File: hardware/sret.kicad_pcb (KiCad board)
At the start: 4 copper layers, 87.9 x 54.4 mm, 105 parts, among them CON1 SD_Card, J1 RJ45-TRANSFO, P1 USB0, P10 CONN_02X04, P11 USB1, P12 CONN_02X01, P13 CONN_02X01, P2 CONN_02X01, P3 CONN_02X01, P4 CONN_02X01, P5 CONN_02X01, P6 CONN_01X06, P7 CONN_01X06, P8 CONN_01X06, P9 CONN_01X06, SW1 DFU, SW2 RESET, U1 LPC4330, U2 DRTR5V0U2SR, U3 W25Q80BV, U4 LAN8742A, U5 MAX3051, U6 MAX3051, U7 TC1262, X1 CRYSTAL_SMD, X2 CRYSTAL_SMD, Y1 RTC

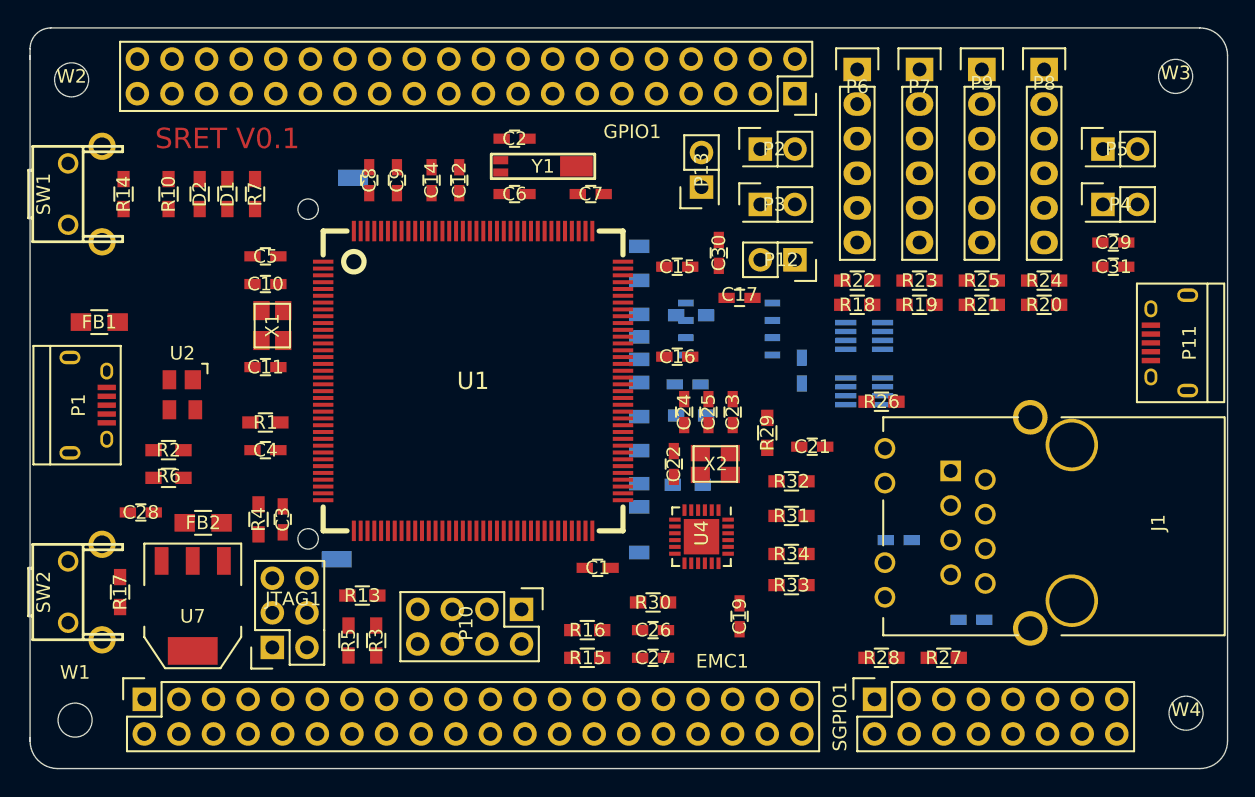
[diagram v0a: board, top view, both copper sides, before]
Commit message: added RS485/IEBus chip
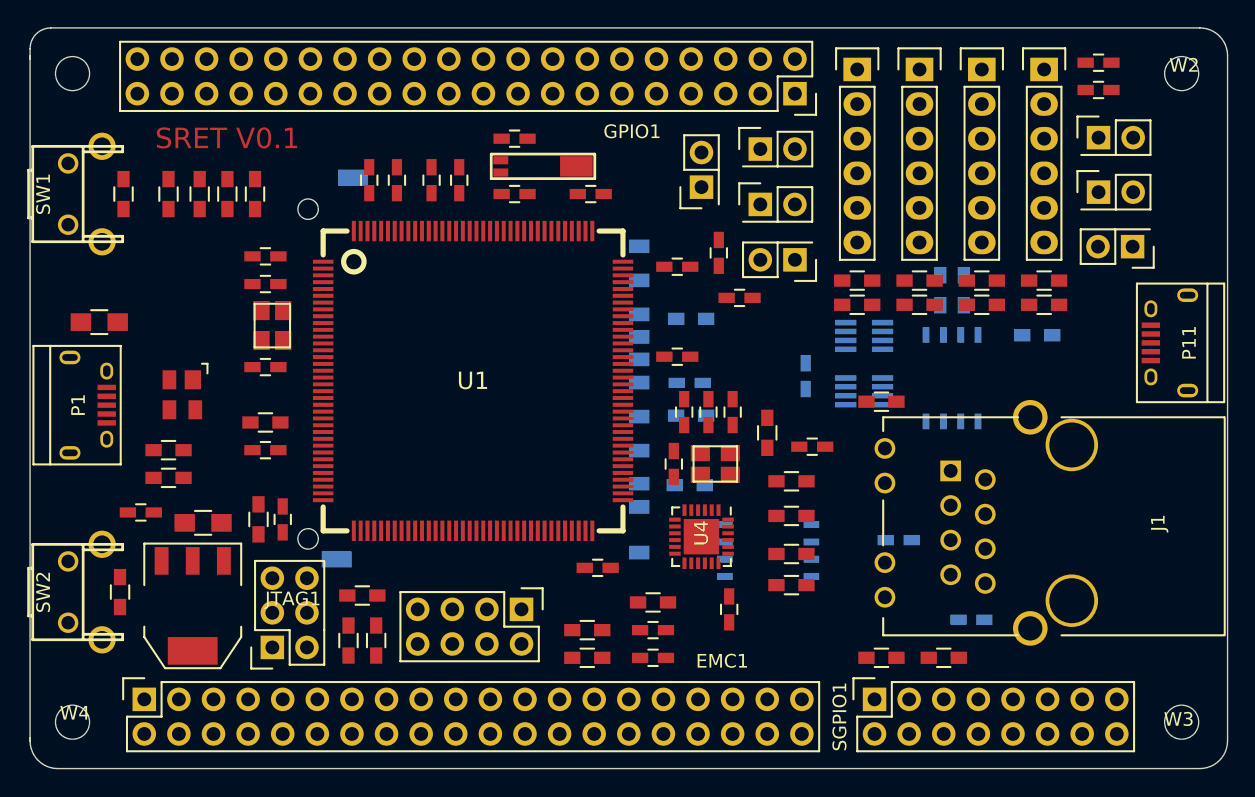
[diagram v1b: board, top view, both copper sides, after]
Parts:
- added P14: CONN_02X01, Pin_Headers:Pin_Header_Straight_2x01, F.Cu at (118.0, 44.5)
- added R12: 10k, Resistors_SMD:R_0603_HandSoldering, B.Cu at (111.0, 51.0)
- added R35: 180, Resistors_SMD:R_0603_HandSoldering, B.Cu at (105.6, 47.7)
- added R36: 180, Resistors_SMD:R_0603_HandSoldering, B.Cu at (103.9, 47.7)
- added U8: RS-485/IEBus, SMD_Packages:SOIC-8-N, B.Cu at (104.7, 54.2)
- moved W4 81.7 mm to (40.2, 79.4)
- moved W2 81.5 mm to (121.6, 31.8)
- moved W1 47.4 mm to (40.2, 31.8)
- moved W3 47.4 mm to (121.6, 79.4)
- moved U3 16.5 mm to (91.2, 66.8)
- moved C31 15.0 mm to (115.5, 31.0), turned to 180 degrees
- moved C29 11.2 mm to (115.5, 33.0), turned to 180 degrees
- moved P4 0.96 mm to (115.5, 40.5)
- moved C19 0.92 mm to (88.4, 71.1)
- moved P5 0.90 mm to (115.5, 36.5)
- moved C13 0.49 mm to (94.0, 54.0)
- moved R8 0.27 mm to (85.6, 49.8)
- moved C32 0.19 mm to (85.5, 54.5)
- moved R11 0.16 mm to (85.5, 62.0)
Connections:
- EMC1 pad 40: GND -> VCC
- GPIO1 pad 23: GND -> /A
- GPIO1 pad 25: /ALARM -> /B
- GPIO1 pad 39: VCC -> GND
- SGPIO1 pad 15: GND -> /ALARM

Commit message: pcb routing started
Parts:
- removed ?: Symbol_OSHW-Logo_SilkScreen, Symbols:Symbol_OSHW-Logo_SilkScreen
- removed EMC1, GPIO1: CONN_02X20, Socket_Strips:Socket_Strip_Straight_2x20
- removed SGPIO1: CONN_02X08, Socket_Strips:Socket_Strip_Straight_2x08
- added EMC: CONN_02X20, Socket_Strips:Socket_Strip_Straight_2x20, F.Cu at (45.3, 78.0)
- added GPIO: CONN_02X20, Socket_Strips:Socket_Strip_Straight_2x20, F.Cu at (45.3, 30.9)
- added SGPIO: CONN_02X08, Socket_Strips:Socket_Strip_Straight_2x08, F.Cu at (98.5, 77.9)
- C1: moved to B.Cu
- P1, P11: footprint Connect:USB_Micro-B -> Connect:USB_Micro-B_circle
- moved U2 4.26 mm to (48.9, 51.1), turned to 270 degrees
- moved C1 2.53 mm to (77.9, 70.5), turned to 270 degrees
- moved R30 1.77 mm to (81.8, 69.1), turned to 270 degrees
- moved R11 1.19 mm to (85.5, 60.8)
- moved C19 1.05 mm to (89.4, 71.5)
- moved C26 0.95 mm to (83.1, 73.5), turned to 0 degrees
- moved R16 0.92 mm to (77.3, 73.3)
- moved C23 0.84 mm to (89.3, 56.1)
- moved R15 0.81 mm to (77.3, 75.2)
- moved X2 0.75 mm to (87.4, 59.7)
- moved C27 0.64 mm to (83.1, 75.2), turned to 0 degrees
- moved SW1 0.62 mm to (40.5, 40.7)
- moved SW2 0.62 mm to (40.5, 69.9)
- moved C11 0.59 mm to (53.8, 53.2)
- moved C10 0.58 mm to (53.8, 47.3), turned to 180 degrees
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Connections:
- U1 pad 7: (no net) -> /GPIO1
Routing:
- net VCC: track 0.00 -> 71.8 mm, vias 0 -> 2
- net /ENET_MDC: track 0.00 -> 42.5 mm, vias 0 -> 4
- net /ENET_TX_EN: track 0.00 -> 41.9 mm, vias 0 -> 4
- net Net-(J1-PadYA): track 0.00 -> 28.1 mm, vias 0 -> 3
- net /ENET_RXD1: track 0.00 -> 27.2 mm
- net Net-(J1-Pad4): track 0.00 -> 23.4 mm, vias 0 -> 1
- net /5V: track 0.00 -> 22.3 mm
- net Net-(J1-Pad6): track 0.00 -> 21.8 mm, vias 0 -> 1
- net Net-(J1-Pad3): track 0.00 -> 21.0 mm
- net Net-(J1-Pad1): track 0.00 -> 20.9 mm
- net /ENET_TXD1: track 0.00 -> 20.8 mm, vias 0 -> 2
- net /ENET_TXD0: track 0.00 -> 20.7 mm, vias 0 -> 4
- net Net-(P1-Pad3): track 0.00 -> 19.8 mm, vias 0 -> 2
- net Net-(P1-Pad2): track 0.00 -> 19.7 mm, vias 0 -> 2
- net Net-(P1-Pad4): track 0.00 -> 19.3 mm, vias 0 -> 2
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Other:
- board text added: "."
- board text added: "1"
- board text added: "2"
- board text added: "3"
- board text added: "4"

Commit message: saving before fix permissions
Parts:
- moved R34 0.96 mm to (93.4, 66.2)
- moved R33 0.70 mm to (93.4, 68.8)
- moved R31 0.45 mm to (93.4, 64.2)
- moved R32 0.45 mm to (93.4, 61.7)
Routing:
- net Net-(J1-Pad1): track 20.9 -> 22.3 mm
- net Net-(J1-Pad6): track 21.8 -> 23.0 mm
- net Net-(J1-Pad4): track 23.4 -> 22.8 mm
- net Net-(J1-Pad3): track 21.0 -> 20.4 mm
- added copper zone on Ground.Plane, net GND
- added copper zone on Power.Plane, net VCC

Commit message: working on traces
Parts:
- moved C31 66.0 mm to (53.5, 53.6)
- moved C30 39.0 mm to (48.7, 48.2), turned to 180 degrees
- moved R12 12.0 mm to (121.0, 44.4), turned to 270 degrees
- moved C11 3.17 mm to (52.2, 50.5), turned to 90 degrees
- moved P5 2.56 mm to (118.0, 36.7), turned to 180 degrees
- moved P4 2.54 mm to (118.0, 40.4), turned to 180 degrees
- moved P14 2.52 mm to (115.5, 44.5), turned to 0 degrees
- moved R7 1.02 mm to (52.8, 40.0)
- moved R10 0.89 mm to (47.9, 40.0)
- moved D1 0.75 mm to (51.2, 40.0)
- moved D2 0.63 mm to (49.5, 40.0)
- moved C16 0.47 mm to (84.6, 52.1)
- moved C10 0.46 mm to (53.3, 47.3)
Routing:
- net GND: track 0.00 -> 73.3 mm, vias 0 -> 17
- net /ADC1: track 0.00 -> 42.8 mm, vias 0 -> 2
- net /ADC6: track 0.00 -> 42.4 mm, vias 0 -> 2
- net /ADC5: track 0.00 -> 40.6 mm, vias 0 -> 4
- net Net-(P11-Pad3): track 0.00 -> 40.4 mm, vias 0 -> 2
- net Net-(P11-Pad2): track 0.00 -> 40.3 mm, vias 0 -> 2
- net /ADC2: track 0.00 -> 39.5 mm, vias 0 -> 2
- net /ADC4: track 0.00 -> 38.4 mm, vias 0 -> 2
- net /GPIO2: track 0.00 -> 37.8 mm, vias 0 -> 2
- net /ADC7: track 0.00 -> 36.0 mm, vias 0 -> 1
- net /ADC3: track 0.00 -> 35.6 mm, vias 0 -> 2
- net /GPIO3: track 0.00 -> 33.3 mm, vias 0 -> 2
- net /GPIO1: track 0.00 -> 32.8 mm, vias 0 -> 2
- net TRST#: track 0.00 -> 30.6 mm, vias 0 -> 1
- net TCK: track 6.28 -> 35.5 mm, vias 0 -> 1
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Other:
- outline, holes or cut-outs redrawn
- board text added: "SRET V_0.1"
- board text removed: "SRET V0.1"

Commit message: 2nd version pcb
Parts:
- removed CON1: SD_Card, Connect:SD_Card_Receptacle
- removed EMC, GPIO: CONN_02X20, Socket_Strips:Socket_Strip_Straight_2x20
- removed R11, R8, R9: 1k5, Resistors_SMD:R_0603_HandSoldering
- removed SGPIO: CONN_02X08, Socket_Strips:Socket_Strip_Straight_2x08
- added EMC1: CONN_02X20, Socket_Strips:Socket_Strip_Straight_2x20, F.Cu at (94.4, 82.0)
- added GPIO1: CONN_02X20, Socket_Strips:Socket_Strip_Straight_2x20, F.Cu at (93.8, 22.6)
- added SGPIO1: CONN_02X08, Socket_Strips:Socket_Strip_Straight_2x08, F.Cu at (117.4, 82.0)
- C1, C32: footprint Capacitors_SMD:C_0603_HandSoldering -> Capacitors_SMD:C_0603; moved to F.Cu
- C10, C11, C12, C13, C14, C15, C16, C17, C18, C19, C2, C20, C21, C22, C23, C28, C29, C3, C30, C31, C4, C5, C6, C7, C8, C9: footprint Capacitors_SMD:C_0603_HandSoldering -> Capacitors_SMD:C_0603
- C24, C25, C26, C27: footprint Capacitors_SMD:C_0603_HandSoldering -> Capacitors_SMD:C_0603; moved to B.Cu
- FB2: moved to B.Cu
- R1, R10, R12, R13, R14, R15, R16, R17, R18, R19, R2, R20, R21, R22, R23, R24, R25, R26, R27, R28, R29, R3, R31, R32, R33, R34, R35, R36, R4, R5, R6, R7: footprint Resistors_SMD:R_0603_HandSoldering -> Resistors_SMD:R_0603
- R30: footprint Resistors_SMD:R_0603_HandSoldering -> Resistors_SMD:R_0603; moved to B.Cu
- moved C29 64.1 mm to (62.6, 69.2), turned to 270 degrees
- moved C32 47.7 mm to (131.8, 43.2)
- moved C17 43.1 mm to (132.2, 46.2)
- moved R14 33.8 mm to (43.4, 74.4)
- moved SW1 33.7 mm to (39.6, 74.4)
- moved U3 32.6 mm to (77.2, 37.4), turned to 270 degrees
- moved R17 30.1 mm to (43.0, 39.8)
- moved SW2 29.9 mm to (40.2, 40.0)
- moved C13 29.5 mm to (71.0, 35.6), turned to 0 degrees
- moved W3 18.1 mm to (136.8, 89.2)
- moved R15 14.8 mm to (62.6, 74.2), turned to 90 degrees
- moved R13 14.5 mm to (75.8, 72.3), turned to 90 degrees
- moved W2 13.8 mm to (130.2, 21.0)
- moved R5 13.8 mm to (48.0, 67.5)
- moved C27 12.5 mm to (83.6, 62.7), turned to 90 degrees
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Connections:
- P9 pad 2: Net-(P9-Pad2) -> /SD_CLK
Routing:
- net VCC: track 99.8 -> 50.7 mm
- net /ADC1: track 42.8 -> 0.00 mm, vias 2 -> 0
- net /ADC6: track 42.4 -> 0.00 mm, vias 2 -> 0
- net /ADC5: track 40.6 -> 0.00 mm, vias 4 -> 0
- net Net-(P11-Pad3): track 40.4 -> 0.00 mm, vias 2 -> 0
- net Net-(P11-Pad2): track 40.3 -> 0.00 mm, vias 2 -> 0
- net /ADC2: track 39.5 -> 0.00 mm, vias 2 -> 0
- net /ADC4: track 38.4 -> 0.00 mm, vias 2 -> 0
- net /GPIO2: track 37.8 -> 0.00 mm, vias 2 -> 0
- net /ADC7: track 36.0 -> 0.00 mm, vias 1 -> 0
- net /RESET#: track 5.55 -> 41.5 mm, vias 0 -> 2
- net /ADC3: track 35.6 -> 0.00 mm, vias 2 -> 0
- net /GPIO3: track 33.3 -> 0.00 mm, vias 2 -> 0
- net /GPIO1: track 32.8 -> 0.00 mm, vias 2 -> 0
- net /GPIO12: track 29.0 -> 0.00 mm, vias 3 -> 0
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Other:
- board outline removed

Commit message: update pcb
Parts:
- C13, C18, C20, C24, C25, C26, C27, FB2, R12, R30, R35, R36, U3, U5, U6, U8: moved to F.Cu
- moved W4 213.8 mm to (246.7, 28.3)
- moved P3 155.5 mm to (246.2, 41.2), turned to 180 degrees
- moved W1 154.8 mm to (163.1, 111.7)
- moved C12 154.6 mm to (222.8, 28.2)
- moved C24 153.0 mm to (237.3, 72.5)
- moved X2 152.8 mm to (240.1, 75.0)
- moved C22 152.7 mm to (240.0, 71.8)
- moved C26 152.4 mm to (234.4, 69.3)
- moved C4 151.9 mm to (203.3, 88.0), turned to 315 degrees
- moved C23 151.7 mm to (240.9, 79.2), turned to 270 degrees
- moved C25 150.0 mm to (235.8, 72.5)
- moved C27 149.4 mm to (232.9, 69.3)
- moved R29 148.3 mm to (237.9, 80.3), turned to 0 degrees
- moved R30 147.9 mm to (231.3, 69.5), turned to 90 degrees
- moved R26 146.6 mm to (241.1, 90.3)
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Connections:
- GPIO1 pad 22: /CANL_0 -> /CANL_1
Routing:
- net GND: track 59.3 -> 0.00 mm, vias 17 -> 0
- net VCC: track 50.7 -> 0.00 mm, vias 10 -> 0
- net /ENET_MDC: track 43.3 -> 0.00 mm, vias 2 -> 0
- net /RESET#: track 41.5 -> 0.00 mm, vias 2 -> 0
- net /ENET_TX_EN: track 37.2 -> 0.00 mm, vias 2 -> 0
- net /ENET_RXD1: track 27.6 -> 0.00 mm, vias 2 -> 0
- net Net-(J1-PadYA): track 23.5 -> 0.00 mm, vias 1 -> 0
- net TCK: track 23.0 -> 0.00 mm, vias 1 -> 0
- net /ENET_TXD1: track 22.0 -> 0.00 mm, vias 2 -> 0
- net /ENET_TXD0: track 21.7 -> 0.00 mm, vias 2 -> 0
- net Net-(J1-Pad4): track 21.6 -> 0.00 mm, vias 1 -> 0
- net Net-(J1-Pad6): track 21.6 -> 0.00 mm, vias 1 -> 0
- net Net-(J1-Pad1): track 20.6 -> 0.00 mm
- net Net-(J1-Pad3): track 19.4 -> 0.00 mm
- net TRST#: track 19.2 -> 0.00 mm, vias 1 -> 0
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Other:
- board text removed: "."

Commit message: pcb edges
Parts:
- moved C3 47.2 mm to (217.8, 79.6), turned to 315 degrees
- moved C29 41.9 mm to (210.8, 85.8), turned to 225 degrees
- moved R14 38.6 mm to (166.8, 58.4)
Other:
- board outline added: 90 x 90 mm
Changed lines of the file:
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@@
   (general
     (links 364)
-    (no_connects 364)
-    (area 0 0 0 0)
+    (no_connects 344)
+    (area 159.949999 24.949999 250.064215 115.050001)
     (thickness 1.6)
-    (drawings 11)
+    (drawings 19)
     (tracks 0)
     (zones 0)
@@
   )
   (module Capacitors_SMD:C_0603 (layer Top)
-    (at 174.1 97.55 270)
+    (at 217.8 79.6 315)
     (descr "Capacitor SMD 0603, reflow soldering, AVX (see smccp.pdf)")
     (tags "capacitor 0603")
     (attr smd)
-    (fp_text reference C3 (at 0 -1.9 270) (layer F.SilkS)
+    (fp_text reference C3 (at 0 -1.9 315) (layer F.SilkS)
       (effects (font (size 1 1) (thickness 0.15)))
     )
-    (fp_text value 100nF (at 0 1.9 270) (layer F.Fab)
+    (fp_text value 100nF (at 0 1.9 315) (layer F.Fab)
       (effects (font (size 1 1) (thickness 0.15)))
     )
@@
     (fp_line (start -0.35 -0.6) (end 0.35 -0.6) (layer F.SilkS) (width 0.15))
     (fp_line (start 0.35 0.6) (end -0.35 0.6) (layer F.SilkS) (width 0.15))
-    (pad 1 smd rect (at -0.75 0 270) (size 0.8 0.75) (layers Top F.Paste F.Mask)
+    (pad 1 smd rect (at -0.75 0 315) (size 0.8 0.75) (layers Top F.Paste F.Mask)
       (net 1 VCC))
-    (pad 2 smd rect (at 0.75 0 270) (size 0.8 0.75) (layers Top F.Paste F.Mask)
+    (pad 2 smd rect (at 0.75 0 315) (size 0.8 0.75) (layers Top F.Paste F.Mask)
       (net 2 GND))
     (model Capacitors_SMD.3dshapes/C_0603.wrl
@@
   )
   (module Capacitors_SMD:C_0603 (layer Top)
-    (at 170.45 97.05 270)
+    (at 210.8 85.8 225)
     (descr "Capacitor SMD 0603, reflow soldering, AVX (see smccp.pdf)")
     (tags "capacitor 0603")
     (attr smd)
-    (fp_text reference C29 (at 0 -1.9 270) (layer F.SilkS)
+    (fp_text reference C29 (at 0 -1.9 225) (layer F.SilkS)
       (effects (font (size 1 1) (thickness 0.15)))
     )
-    (fp_text value 100nF (at 0 1.9 270) (layer F.Fab)
+    (fp_text value 100nF (at 0 1.9 225) (layer F.Fab)
       (effects (font (size 1 1) (thickness 0.15)))
     )
@@
     (fp_line (start -0.35 -0.6) (end 0.35 -0.6) (layer F.SilkS) (width 0.15))
     (fp_line (start 0.35 0.6) (end -0.35 0.6) (layer F.SilkS) (width 0.15))
-    (pad 1 smd rect (at -0.75 0 270) (size 0.8 0.75) (layers Top F.Paste F.Mask)
+    (pad 1 smd rect (at -0.75 0 225) (size 0.8 0.75) (layers Top F.Paste F.Mask)
       (net 1 VCC))
-    (pad 2 smd rect (at 0.75 0 270) (size 0.8 0.75) (layers Top F.Paste F.Mask)
+    (pad 2 smd rect (at 0.75 0 225) (size 0.8 0.75) (layers Top F.Paste F.Mask)
       (net 2 GND))
     (model Capacitors_SMD.3dshapes/C_0603.wrl
@@
   )
   (module Resistors_SMD:R_0603 (layer Top)
-    (at 166.3 97 90)
+    (at 166.8 58.4 90)
     (descr "Resistor SMD 0603, reflow soldering, Vishay (see dcrcw.pdf)")
     (tags "resistor 0603")
@@
     )
   )
+  (gr_line (start 250 113.4) (end 250 26.4) (angle 90) (layer Edge.Cuts) (width 0.1))
+  (gr_line (start 161.4 115) (end 248.8 115) (angle 90) (layer Edge.Cuts) (width 0.1))
+  (gr_line (start 160 26.4) (end 160 113.6) (angle 90) (layer Edge.Cuts) (width 0.1))
+  (gr_line (start 248.6 25) (end 161.4 25) (angle 90) (layer Edge.Cuts) (width 0.1))
+  (gr_arc (start 248.6 26.4) (end 248.6 25) (angle 90) (layer Edge.Cuts) (width 0.1))
+  (gr_arc (start 161.4 26.4) (end 160 26.4) (angle 90) (layer Edge.Cuts) (width 0.1))
+  (gr_arc (start 161.4 113.6) (end 161.4 115) (angle 90) (layer Edge.Cuts) (width 0.1))
+  (gr_arc (start 248.6 113.6) (end 250 113.4) (angle 90) (layer Edge.Cuts) (width 0.1))
+  (gr_text 3 (at 165.45 104.75) (layer Power.Plane)
+    (effects (font (size 1.5 1.5) (thickness 0.3)))
+  )
+  (gr_text 2 (at 163.6 104.65) (layer Ground.Plane)
+    (effects (font (size 1.5 1.5) (thickness 0.3)))
+  )
   (gr_line (start 250 25) (end 160 25) (angle 90) (layer Eco1.User) (width 0.2))
   (gr_line (start 250 115) (end 250 25) (angle 90) (layer Eco1.User) (width 0.2))
@@
     (effects (font (size 1.5 1.5) (thickness 0.3)))
   )
-  (gr_text 3 (at 42.2 47.2) (layer Power.Plane)
-    (effects (font (size 1.5 1.5) (thickness 0.3)))
-  )
-  (gr_text 2 (at 40.4 47.2) (layer Ground.Plane)
-    (effects (font (size 1.5 1.5) (thickness 0.3)))
-  )
   (gr_text 1 (at 161.9 104.65) (layer Top)
     (effects (font (size 1.5 1.5) (thickness 0.3)))
   )
-  (gr_text thejamestate@gmail.com (at 229.85 110.35) (layer B.SilkS)
+  (gr_text thejamestate@gmail.com (at 230.45 106.9) (layer B.SilkS)
     (effects (font (size 1.5 1.5) (thickness 0.3)) (justify mirror))
   )
-  (gr_text www.hwreblog.com (at 231.7 107.3) (layer B.SilkS)
+  (gr_text www.hwreblog.com (at 231.8 109.3) (layer B.SilkS)
     (effects (font (size 1.5 1.5) (thickness 0.3)) (justify mirror))
   )
@@
     (effects (font (size 1.5 1.5) (thickness 0.3)))
   )
-  (zone (net 2) (net_name GND) (layer Ground.Plane) (hatch edge 0.508)
+  (zone (net 0) (net_name "") (layer Top) (hatch edge 0.508)
     (connect_pads (clearance 0.25))
     (min_thickness 0.254)
-    (fill yes (arc_segments 16) (thermal_gap 0.25) (thermal_bridge_width 0.508))
+    (keepout (tracks not_allowed) (vias not_allowed) (copperpour not_allowed))
+    (fill (arc_segments 16) (thermal_gap 0.25) (thermal_bridge_width 0.508))
     (polygon
       (pts
-        (xy 34.4 27.6) (xy 127.6 27.6) (xy 127.8 87.4) (xy 34.2 87.4) (xy 34.4 27.6)
+        (xy 168.1 105.85) (xy 161.1 105.85) (xy 161.1 103.45) (xy 168.1 103.45) (xy 168.1 105.85)
       )
     )
   )
-  (zone (net 1) (net_name VCC) (layer Power.Plane) (hatch edge 0.508)
-    (connect_pads (clearance 0.25))
+  (zone (net 2) (net_name GND) (layer Ground.Plane) (hatch edge 0.508)
+    (connect_pads (clearance 0.508))
     (min_thickness 0.254)
-    (fill yes (arc_segments 16) (thermal_gap 0.25) (thermal_bridge_width 0.508))
+    (fill yes (arc_segments 16) (thermal_gap 0.508) (thermal_bridge_width 0.508))
     (polygon
       (pts
-        (xy 34.4 27.6) (xy 127.6 27.6) (xy 127.8 87.4) (xy 34.2 87.4) (xy 34.4 27.6)
+        (xy 254.3 121.3) (xy 156.8 121.3) (xy 156.8 21.7) (xy 254.3 21.7) (xy 254.3 121.3)
       )
     )
   )
-  (zone (net 0) (net_name "") (layer Top) (hatch edge 0.508)
-    (connect_pads (clearance 0.25))
+  (zone (net 1) (net_name VCC) (layer Power.Plane) (hatch edge 0.508)
+    (connect_pads (clearance 0.508))
     (min_thickness 0.254)
-    (keepout (tracks not_allowed) (vias not_allowed) (copperpour not_allowed))
-    (fill (arc_segments 16) (thermal_gap 0.25) (thermal_bridge_width 0.508))
+    (fill yes (arc_segments 16) (thermal_gap 0.508) (thermal_bridge_width 0.508))
     (polygon
       (pts
-        (xy 168.1 105.85) (xy 161.1 105.85) (xy 161.1 103.45) (xy 168.1 103.45) (xy 168.1 105.85)
+        (xy 156.8 21.7) (xy 254.3 21.7) (xy 254.3 121.3) (xy 156.8 121.3) (xy 156.8 121.2)
       )
     )
   )
-  (zone (net 0) (net_name "") (layer Ground.Plane) (hatch edge 0.508)
-    (connect_pads (clearance 0.25))
+  (zone (net 0) (net_name "") (layer Power.Plane) (hatch edge 0.508)
+    (connect_pads (clearance 0.508))
     (min_thickness 0.254)
     (keepout (tracks not_allowed) (vias not_allowed) (copperpour not_allowed))
-    (fill (arc_segments 16) (thermal_gap 0.25) (thermal_bridge_width 0.508))
+    (fill (arc_segments 16) (thermal_gap 0.508) (thermal_bridge_width 0.508))
     (polygon
       (pts
-        (xy 44.8 48.4) (xy 37.8 48.4) (xy 37.8 46) (xy 44.8 46) (xy 44.8 48.4)
+        (xy 168.1 105.85) (xy 161.1 105.85) (xy 161.1 103.45) (xy 168.1 103.45) (xy 168.1 105.85)
       )
     )
   )
-  (zone (net 0) (net_name "") (layer Power.Plane) (hatch edge 0.508)
-    (connect_pads (clearance 0.25))
+  (zone (net 0) (net_name "") (layer Ground.Plane) (hatch edge 0.508)
+    (connect_pads (clearance 0.508))
     (min_thickness 0.254)
     (keepout (tracks not_allowed) (vias not_allowed) (copperpour not_allowed))
-    (fill (arc_segments 16) (thermal_gap 0.25) (thermal_bridge_width 0.508))
+    (fill (arc_segments 16) (thermal_gap 0.508) (thermal_bridge_width 0.508))
     (polygon
       (pts
-        (xy 44.8 48.4) (xy 37.8 48.4) (xy 37.8 46) (xy 44.8 46) (xy 44.8 48.4)
+        (xy 168.1 105.85) (xy 161.1 105.85) (xy 161.1 103.45) (xy 168.1 103.45) (xy 168.1 105.85)
       )
     )
